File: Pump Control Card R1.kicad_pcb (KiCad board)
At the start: 2 copper layers, 65 x 41 mm, 116 parts, among them J1 Conn_01x04, J10 10018784-10201TLF, J2 Conn_01x04, J3 FTSH-107-01-L-D-K, J4 Conn_01x04, J5 Conn_01x04, J6 Conn_01x04, J7 Conn_01x04, J8 Conn_01x04, J9 Conn_01x04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

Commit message: Updated
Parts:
- added R7: 33K, Resistor_SMD:R_0805_2012Metric, F.Cu at (103.9, 71.5)
- added R8: 20K, Resistor_SMD:R_0805_2012Metric, F.Cu at (103.9, 73.4)
- C7, C8: moved to B.Cu
- moved C7 2.24 mm to (102.9, 73.5)
- moved C8 2.24 mm to (102.9, 71.5)
- moved J1 0.50 mm to (94.1, 55.5)
- moved J2 0.50 mm to (101.9, 55.5)
- moved J4 0.50 mm to (109.7, 55.5)
- moved J5 0.50 mm to (117.5, 55.5)
- moved J6 0.50 mm to (125.3, 55.5)
- moved J7 0.50 mm to (133.1, 55.5)
- moved J8 0.50 mm to (140.9, 55.5)
- moved J9 0.50 mm to (148.7, 55.5)
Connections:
- U4 pad 10: /MCU/PA0 -> /MCU/VSENS
- U4 pad 26: /Level Shifter/IN0 -> /Level Shifter/IN1
- U4 pad 28: /Level Shifter/IN1 -> /Level Shifter/IN0
- U5 pad 10: /MCU/PA0 -> /MCU/PA1
- U5 pad 12: /MCU/PA1 -> /MCU/PB3
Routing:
- net /MCU/PB3: track 0.00 -> 30.6 mm, vias 0 -> 4
- net /MCU/PA0: track 30.6 -> 0.00 mm, vias 4 -> 0
- net /MCU/VSENS: track 0.00 -> 17.1 mm, vias 0 -> 2
- net /MCU/PA1: track 35.5 -> 30.8 mm
- net /Level Shifter/IN1: track 37.3 -> 41.2 mm
- net GND: track 116.6 -> 113.2 mm
- net +5V: track 132.2 -> 133.3 mm
- net /Level Shifter/IN0: track 36.6 -> 35.7 mm
- net /SPD_7: track 2.88 -> 3.49 mm
- net /EN_5: track 31.2 -> 31.7 mm
- net /SPD_8: track 2.88 -> 3.38 mm
- net /SPD_6: track 2.88 -> 3.38 mm
- net /SPD_5: track 2.88 -> 3.38 mm
- net /SPD_4: track 2.88 -> 3.38 mm
- net /SPD_3: track 2.88 -> 3.38 mm
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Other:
- board size 65 x 41 mm -> 65 x 41.6 mm

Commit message: Final updates for R2
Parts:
- added C3: 47nF, Capacitor_SMD:C_0805_2012Metric, F.Cu at (103.9, 70.2)
- moved R7 0.70 mm to (103.9, 72.2)
- moved R8 0.70 mm to (103.9, 74.1)
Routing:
- net /MCU/VSENS: track 17.1 -> 18.6 mm
- net GND: track 113.2 -> 111.8 mm, vias 65 -> 66
- net +5V: track 133.3 -> 133.6 mm, vias 16 -> 17

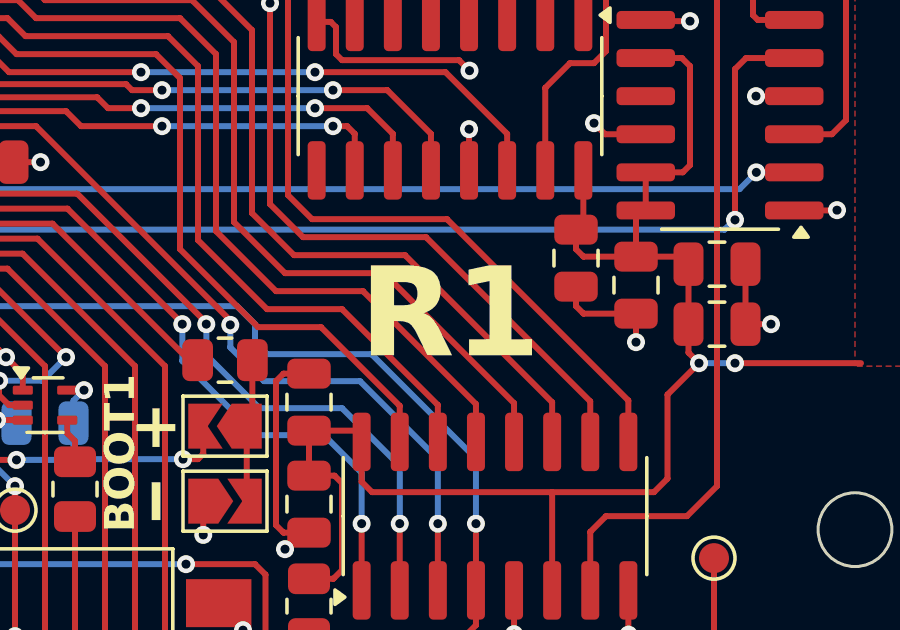
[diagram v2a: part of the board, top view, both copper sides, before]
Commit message: Updated silkscreen
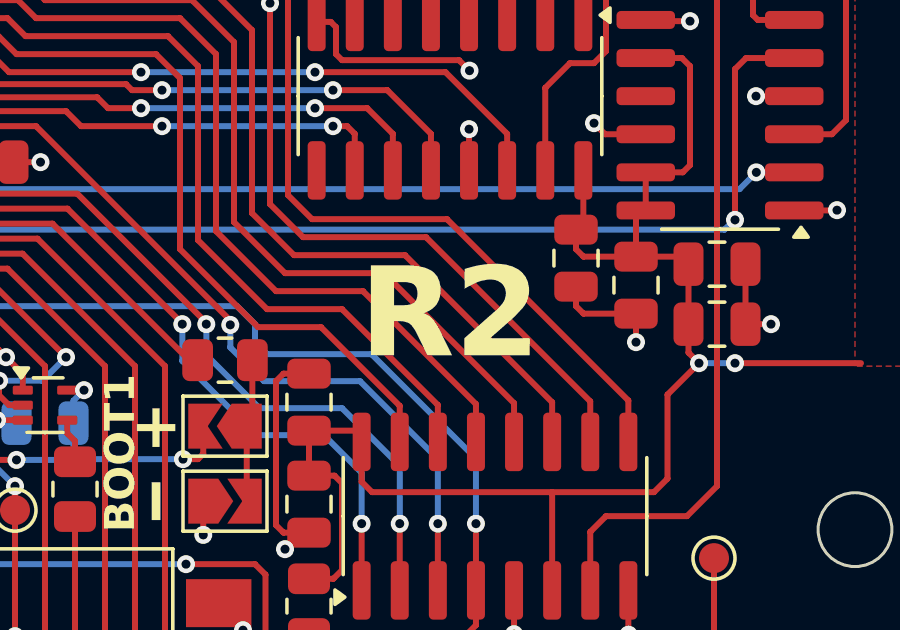
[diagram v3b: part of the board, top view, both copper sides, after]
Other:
- board text added: "R2"
- board text removed: "R1"
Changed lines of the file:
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@@
 		)
 	)
-	(gr_text "R1"
+	(gr_text "R2"
 		(at 136 79.25 0)
 		(layer "F.SilkS")
@@
 			)
 		)
-		(render_cache "R1" 0
+		(render_cache "R2" 0
 			(polygon
 				(pts
@@
 			(polygon
 				(pts
-					(xy 137.931473 77.521587) (xy 137.343458 77.521587) (xy 136.373325 78.340594) (xy 136.730347 78.752021)
-					(xy 137.326788 78.227205) (xy 137.326788 80.495) (xy 137.931473 80.495)
+					(xy 137.410686 77.470296) (xy 137.271687 77.47613) (xy 137.140862 77.493523) (xy 137.023472 77.520902)
+					(xy 136.914344 77.558612) (xy 136.817576 77.604459) (xy 136.729103 77.659585) (xy 136.651481 77.721831)
+					(xy 136.582271 77.792575) (xy 136.522578 77.8705) (xy 136.471629 77.956452) (xy 136.396923 78.152626)
+					(xy 136.360686 78.381994) (xy 136.990649 78.428155) (xy 137.003631 78.34914) (xy 137.027043 78.277954)
+					(xy 137.059344 78.216562) (xy 137.10031 78.163853) (xy 137.148263 78.121184) (xy 137.203325 78.087992)
+					(xy 137.264496 78.064949) (xy 137.3315 78.052371) (xy 137.377164 78.050068) (xy 137.513098 78.072527)
+					(xy 137.574961 78.099969) (xy 137.629709 78.137189) (xy 137.674161 78.181657) (xy 137.708784 78.233812)
+					(xy 137.730916 78.289061) (xy 137.741735 78.349878) (xy 137.742612 78.373567) (xy 137.736074 78.44461)
+					(xy 137.713753 78.51354) (xy 137.630287 78.637791) (xy 137.477914 78.789391) (xy 136.32295 79.827301)
+					(xy 136.32295 80.495) (xy 138.397671 80.495) (xy 138.397671 79.94069) (xy 137.078943 79.94069)
+					(xy 137.918833 79.218037) (xy 138.072894 79.075207) (xy 138.193116 78.938771) (xy 138.254584 78.848174)
+					(xy 138.302657 78.753902) (xy 138.335031 78.663278) (xy 138.357203 78.565656) (xy 138.372575 78.365141)
+					(xy 138.366788 78.24922) (xy 138.349723 78.140443) (xy 138.322391 78.040693) (xy 138.285017 77.948256)
+					(xy 138.238443 77.863991) (xy 138.18282 77.787322) (xy 138.045403 77.657057) (xy 137.873315 77.558472)
+					(xy 137.66643 77.494627) (xy 137.425274 77.470369)
 				)
 			)

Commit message: Library updates
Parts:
- J3: footprint Connector_Samtec:SAMTEC_FTSH-107-01-L-D-K -> Footprints:SAMTEC_FTSH-107-01-L-D-K
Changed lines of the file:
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@@
 		)
 	)
-	(footprint "Connector_Samtec:SAMTEC_FTSH-107-01-L-D-K"
+	(footprint "Footprints:SAMTEC_FTSH-107-01-L-D-K"
 		(layer "F.Cu")
 		(at 95.5 82.4 -90)
 		(property "Reference" "J3"
-			(at -1.48 -4.425 90)
+			(at -1.48 -4.425 270)
 			(layer "F.SilkS")
 			(hide yes)
@@
 		)
 		(property "Value" "FTSH-107-01-L-D-K"
-			(at 10.585 4.425 90)
+			(at 10.585 4.425 270)
 			(layer "F.Fab")
 			(hide yes)
@@
 		(property "Datasheet" ""
 			(at 0 0 270)
-			(unlocked yes)
 			(layer "F.Fab")
 			(hide yes)
@@
 		(property "Description" ""
 			(at 0 0 270)
-			(unlocked yes)
 			(layer "F.Fab")
 			(hide yes)
@@
 		)
 		(embedded_fonts no)
-		(model "/Users/frankzhang/Documents/KiCad/9.0/3dmodels/FTSH-107-01-L-D-K.step"
+		(model "${KIPRJMOD}/Models/FTSH-107-01-L-D-K.step"
 			(offset
 				(xyz 0 0 0)
-			)
-			(scale
-				(xyz 1 1 1)
-			)
-			(rotate
-				(xyz -90 -0 -0)
-			)
-		)
-		(model "C:/Users/Frank/Documents/KiCad/9.0/3dmodels/FTSH-107-01-L-D-K.step"
-			(offset
-				(xyz 0 0 0)
